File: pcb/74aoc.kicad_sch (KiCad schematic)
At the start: 0 parts

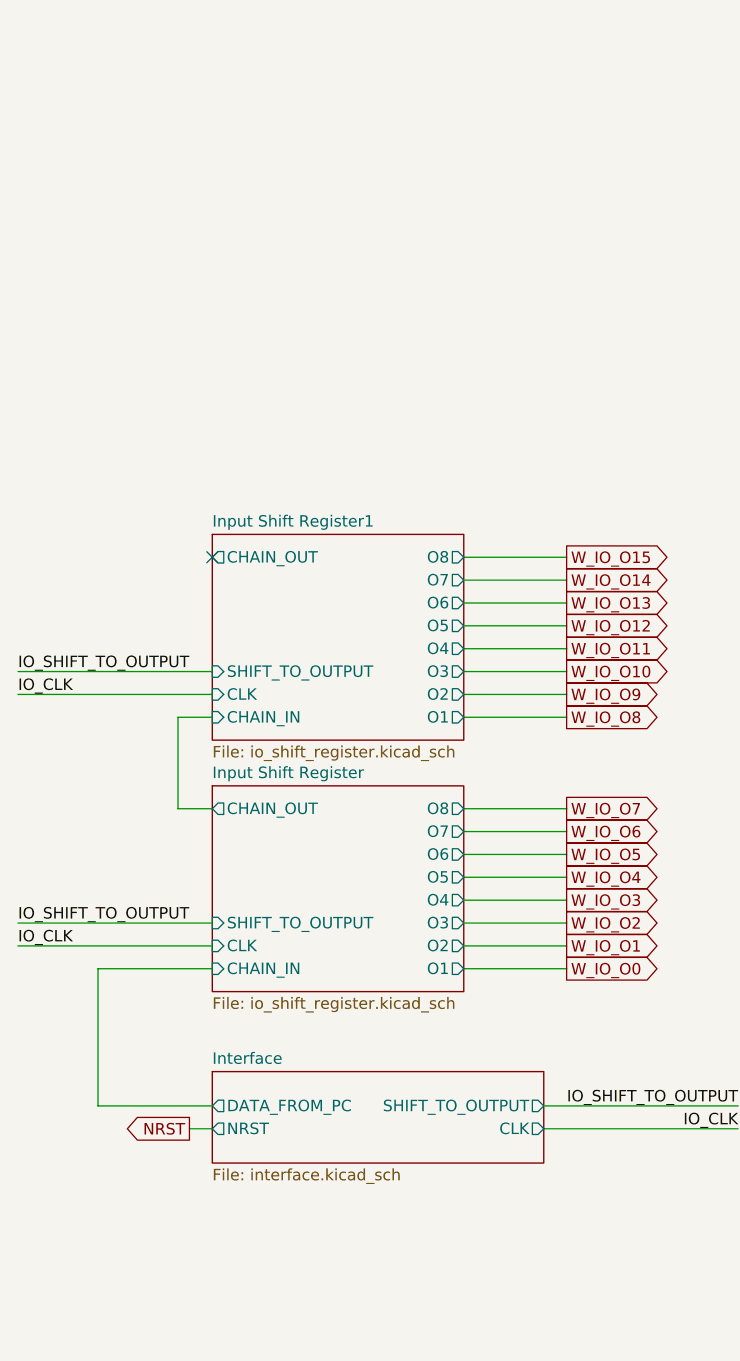
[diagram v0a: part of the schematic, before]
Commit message: Add output LED array
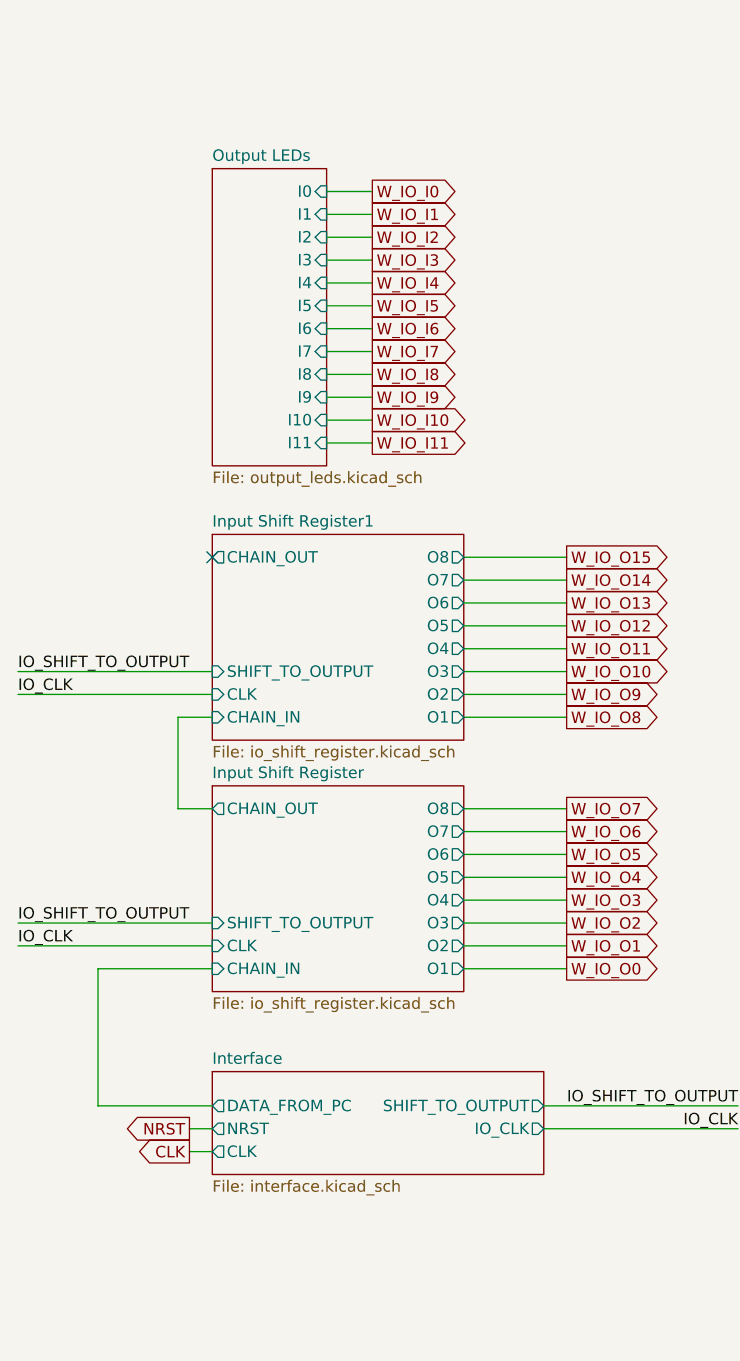
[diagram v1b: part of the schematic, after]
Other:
- added sheet Output LEDs (output_leds.kicad_sch)
- sheet Interface ports: added IO_CLK; removed none

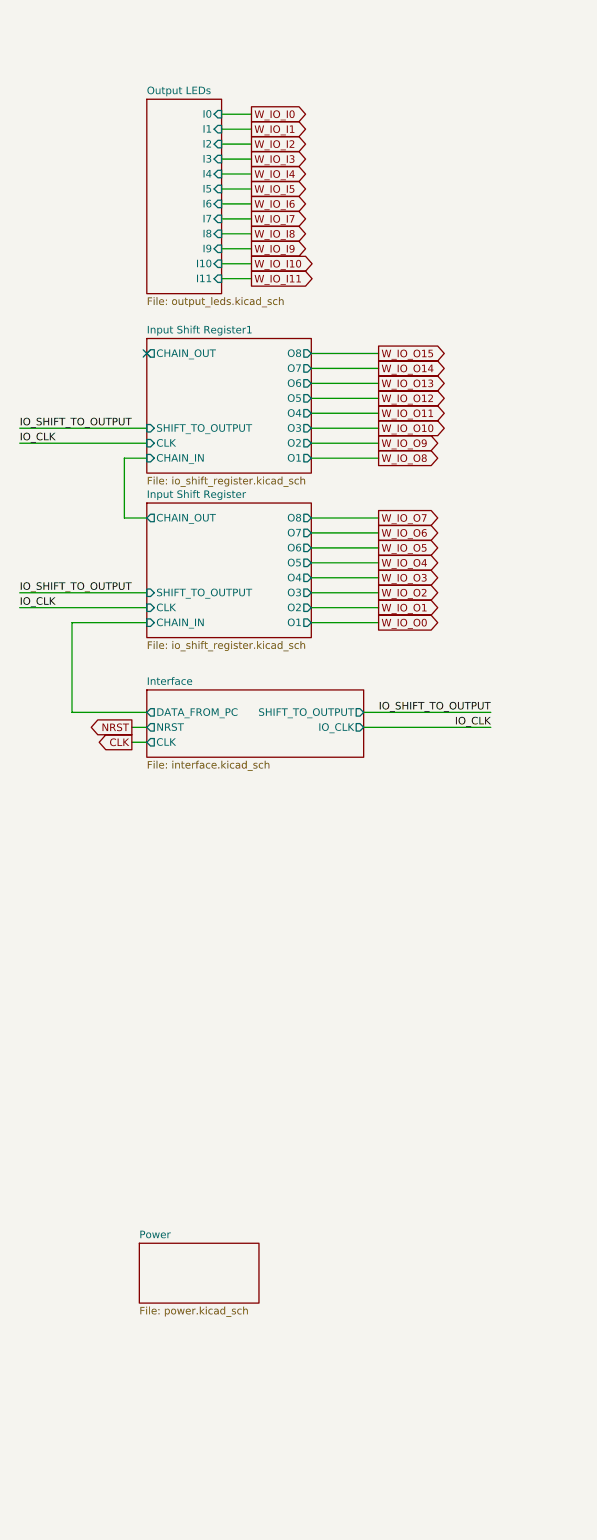
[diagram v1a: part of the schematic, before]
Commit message: Remove IO shift registers
Too complex
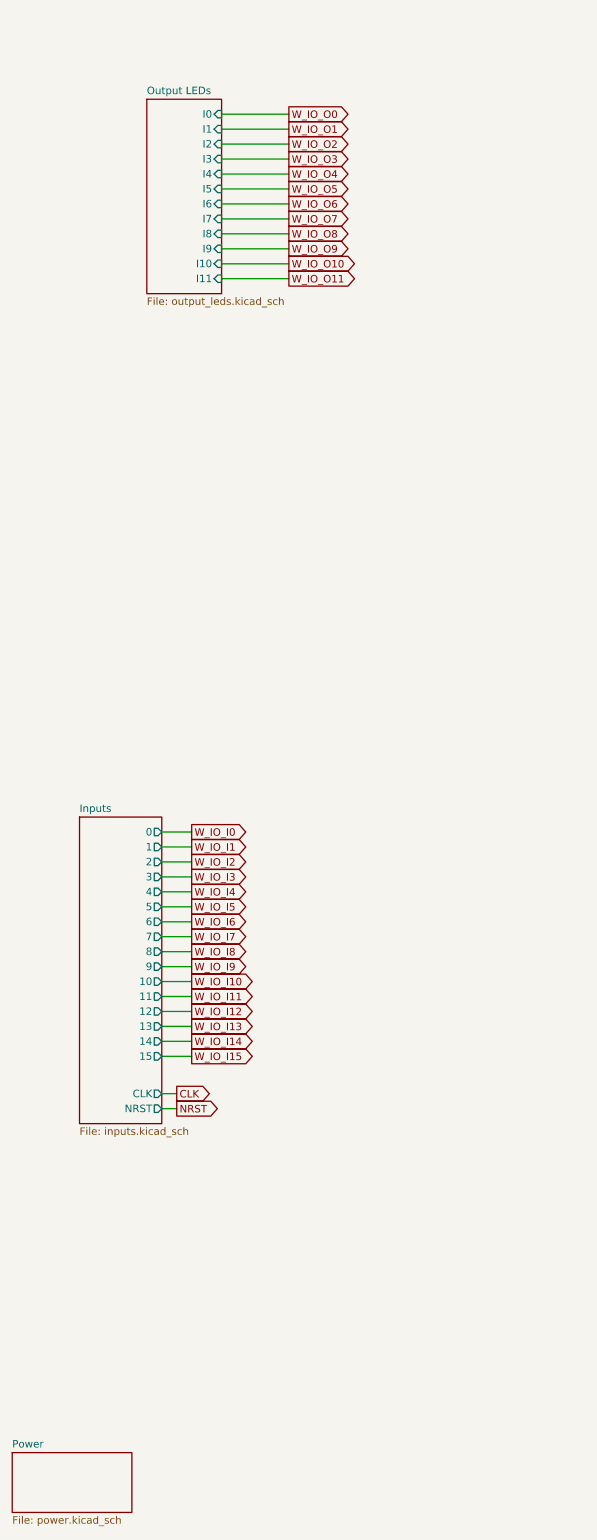
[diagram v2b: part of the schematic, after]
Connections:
- no-connect marks 1 -> 0
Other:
- removed sheet Input Shift Register
- removed sheet Input Shift Register1
- removed sheet Interface
- added sheet Inputs (inputs.kicad_sch)

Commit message: Create a script that duplicates the cell schematic instances
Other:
- added sheet CELL X0 Y1 (cell.kicad_sch)
- added sheet CELL X0 Y10 (cell.kicad_sch)
- added sheet CELL X0 Y2 (cell.kicad_sch)
- added sheet CELL X0 Y3 (cell.kicad_sch)
- added sheet CELL X0 Y4 (cell.kicad_sch)
- added sheet CELL X0 Y5 (cell.kicad_sch)
- added sheet CELL X0 Y6 (cell.kicad_sch)
- added sheet CELL X0 Y7 (cell.kicad_sch)
- added sheet CELL X0 Y8 (cell.kicad_sch)
- added sheet CELL X0 Y9 (cell.kicad_sch)
- added sheet CELL X1 Y0 (cell.kicad_sch)
- added sheet CELL X1 Y1 (cell.kicad_sch)
- added sheet CELL X1 Y10 (cell.kicad_sch)
- added sheet CELL X1 Y2 (cell.kicad_sch)
- added sheet CELL X1 Y3 (cell.kicad_sch)
- added sheet CELL X1 Y4 (cell.kicad_sch)
- added sheet CELL X1 Y5 (cell.kicad_sch)
- added sheet CELL X1 Y6 (cell.kicad_sch)
- added sheet CELL X1 Y7 (cell.kicad_sch)
- added sheet CELL X1 Y8 (cell.kicad_sch)
- added sheet CELL X1 Y9 (cell.kicad_sch)
- added sheet CELL X10 Y0 (cell.kicad_sch)
- added sheet CELL X10 Y1 (cell.kicad_sch)
- added sheet CELL X10 Y10 (cell.kicad_sch)
- added sheet CELL X10 Y2 (cell.kicad_sch)
- added sheet CELL X10 Y3 (cell.kicad_sch)
- added sheet CELL X10 Y4 (cell.kicad_sch)
- added sheet CELL X10 Y5 (cell.kicad_sch)
- added sheet CELL X10 Y6 (cell.kicad_sch)
- added sheet CELL X10 Y7 (cell.kicad_sch)
- added sheet CELL X10 Y8 (cell.kicad_sch)
- added sheet CELL X10 Y9 (cell.kicad_sch)
- added sheet CELL X2 Y0 (cell.kicad_sch)
- added sheet CELL X2 Y1 (cell.kicad_sch)
- added sheet CELL X2 Y10 (cell.kicad_sch)
- added sheet CELL X2 Y2 (cell.kicad_sch)
- added sheet CELL X2 Y3 (cell.kicad_sch)
- added sheet CELL X2 Y4 (cell.kicad_sch)
- added sheet CELL X2 Y5 (cell.kicad_sch)
- added sheet CELL X2 Y6 (cell.kicad_sch)
- added sheet CELL X2 Y7 (cell.kicad_sch)
- added sheet CELL X2 Y8 (cell.kicad_sch)
- added sheet CELL X2 Y9 (cell.kicad_sch)
- added sheet CELL X3 Y0 (cell.kicad_sch)
- added sheet CELL X3 Y1 (cell.kicad_sch)
- added sheet CELL X3 Y10 (cell.kicad_sch)
- added sheet CELL X3 Y2 (cell.kicad_sch)
- added sheet CELL X3 Y3 (cell.kicad_sch)
- added sheet CELL X3 Y4 (cell.kicad_sch)
- added sheet CELL X3 Y5 (cell.kicad_sch)
- added sheet CELL X3 Y6 (cell.kicad_sch)
- added sheet CELL X3 Y7 (cell.kicad_sch)
- added sheet CELL X3 Y8 (cell.kicad_sch)
- added sheet CELL X3 Y9 (cell.kicad_sch)
- added sheet CELL X4 Y0 (cell.kicad_sch)
- added sheet CELL X4 Y1 (cell.kicad_sch)
- added sheet CELL X4 Y10 (cell.kicad_sch)
- added sheet CELL X4 Y2 (cell.kicad_sch)
- added sheet CELL X4 Y3 (cell.kicad_sch)
- added sheet CELL X4 Y4 (cell.kicad_sch)
- added sheet CELL X4 Y5 (cell.kicad_sch)
- added sheet CELL X4 Y6 (cell.kicad_sch)
- added sheet CELL X4 Y7 (cell.kicad_sch)
- added sheet CELL X4 Y8 (cell.kicad_sch)
- added sheet CELL X4 Y9 (cell.kicad_sch)
- added sheet CELL X5 Y0 (cell.kicad_sch)
- added sheet CELL X5 Y1 (cell.kicad_sch)
- added sheet CELL X5 Y10 (cell.kicad_sch)
- added sheet CELL X5 Y2 (cell.kicad_sch)
- added sheet CELL X5 Y3 (cell.kicad_sch)
- added sheet CELL X5 Y4 (cell.kicad_sch)
- added sheet CELL X5 Y5 (cell.kicad_sch)
- added sheet CELL X5 Y6 (cell.kicad_sch)
- added sheet CELL X5 Y7 (cell.kicad_sch)
- added sheet CELL X5 Y8 (cell.kicad_sch)
- added sheet CELL X5 Y9 (cell.kicad_sch)
- added sheet CELL X6 Y0 (cell.kicad_sch)
- added sheet CELL X6 Y1 (cell.kicad_sch)
- added sheet CELL X6 Y10 (cell.kicad_sch)
- added sheet CELL X6 Y2 (cell.kicad_sch)
- added sheet CELL X6 Y3 (cell.kicad_sch)
- added sheet CELL X6 Y4 (cell.kicad_sch)
- added sheet CELL X6 Y5 (cell.kicad_sch)
- added sheet CELL X6 Y6 (cell.kicad_sch)
- added sheet CELL X6 Y7 (cell.kicad_sch)
- added sheet CELL X6 Y8 (cell.kicad_sch)
- added sheet CELL X6 Y9 (cell.kicad_sch)
- added sheet CELL X7 Y0 (cell.kicad_sch)
- added sheet CELL X7 Y1 (cell.kicad_sch)
- added sheet CELL X7 Y10 (cell.kicad_sch)
- added sheet CELL X7 Y2 (cell.kicad_sch)
- added sheet CELL X7 Y3 (cell.kicad_sch)
- added sheet CELL X7 Y4 (cell.kicad_sch)
- added sheet CELL X7 Y5 (cell.kicad_sch)
- added sheet CELL X7 Y6 (cell.kicad_sch)
- added sheet CELL X7 Y7 (cell.kicad_sch)
- added sheet CELL X7 Y8 (cell.kicad_sch)
- added sheet CELL X7 Y9 (cell.kicad_sch)
- added sheet CELL X8 Y0 (cell.kicad_sch)
- added sheet CELL X8 Y1 (cell.kicad_sch)
- added sheet CELL X8 Y10 (cell.kicad_sch)
- added sheet CELL X8 Y2 (cell.kicad_sch)
- added sheet CELL X8 Y3 (cell.kicad_sch)
- added sheet CELL X8 Y4 (cell.kicad_sch)
- added sheet CELL X8 Y5 (cell.kicad_sch)
- added sheet CELL X8 Y6 (cell.kicad_sch)
- added sheet CELL X8 Y7 (cell.kicad_sch)
- added sheet CELL X8 Y8 (cell.kicad_sch)
- added sheet CELL X8 Y9 (cell.kicad_sch)
- added sheet CELL X9 Y0 (cell.kicad_sch)
- added sheet CELL X9 Y1 (cell.kicad_sch)
- added sheet CELL X9 Y10 (cell.kicad_sch)
- added sheet CELL X9 Y2 (cell.kicad_sch)
- added sheet CELL X9 Y3 (cell.kicad_sch)
- added sheet CELL X9 Y4 (cell.kicad_sch)
- added sheet CELL X9 Y5 (cell.kicad_sch)
- added sheet CELL X9 Y6 (cell.kicad_sch)
- added sheet CELL X9 Y7 (cell.kicad_sch)
- added sheet CELL X9 Y8 (cell.kicad_sch)
- added sheet CELL X9 Y9 (cell.kicad_sch)
